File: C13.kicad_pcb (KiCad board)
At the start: 2 copper layers, 80 x 40.1 mm, 120 parts, among them IC1 74HC595BQ,115, IC2 MPM3610AGQV-P, IC9 THVD1450DRBR, J1 V24, J2 Conn_02x04, J3 Conn_02x03, J4 Screw_Terminal_01x04, J5 UDPI, J6 Screw_Terminal_01x04, J7 Screw_Terminal_01x02, K1 G6K-2, Q1 BC848W, Q5 BC857BS, U1 AVR-64DA48, U10 INA181-A1, U11 INA381, U12 INA381, U13 INA181-A1, U14 INA381, U15 INA381, U16 INA181-A4, U2 MIC5235-3.3, U3 INA181-A1, U4 KA78M05_TO252, U5 INA381, U6 INA381, U7 INA181-A1, U8 INA381-A2, U9 INA381, X1 ASE-xxxMHz

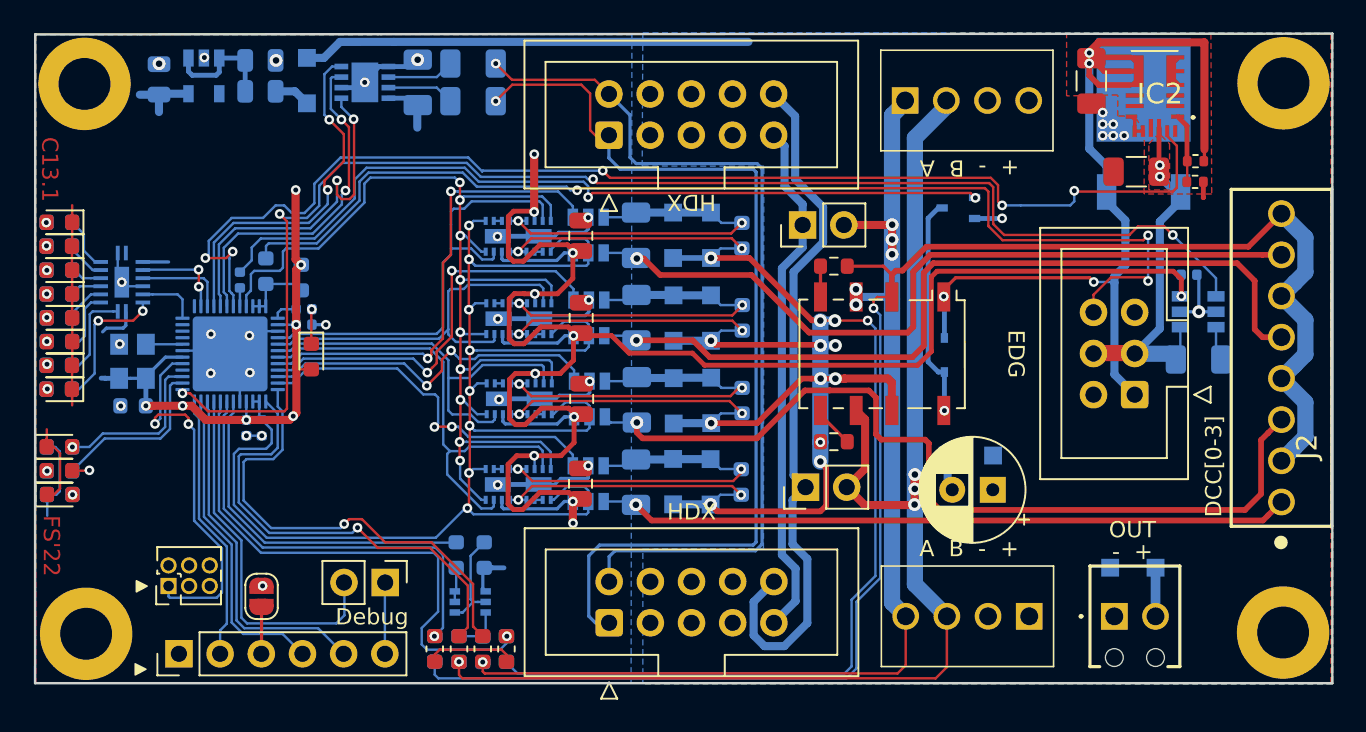
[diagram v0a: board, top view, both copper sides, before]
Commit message: mod: conversion to KiCad 9
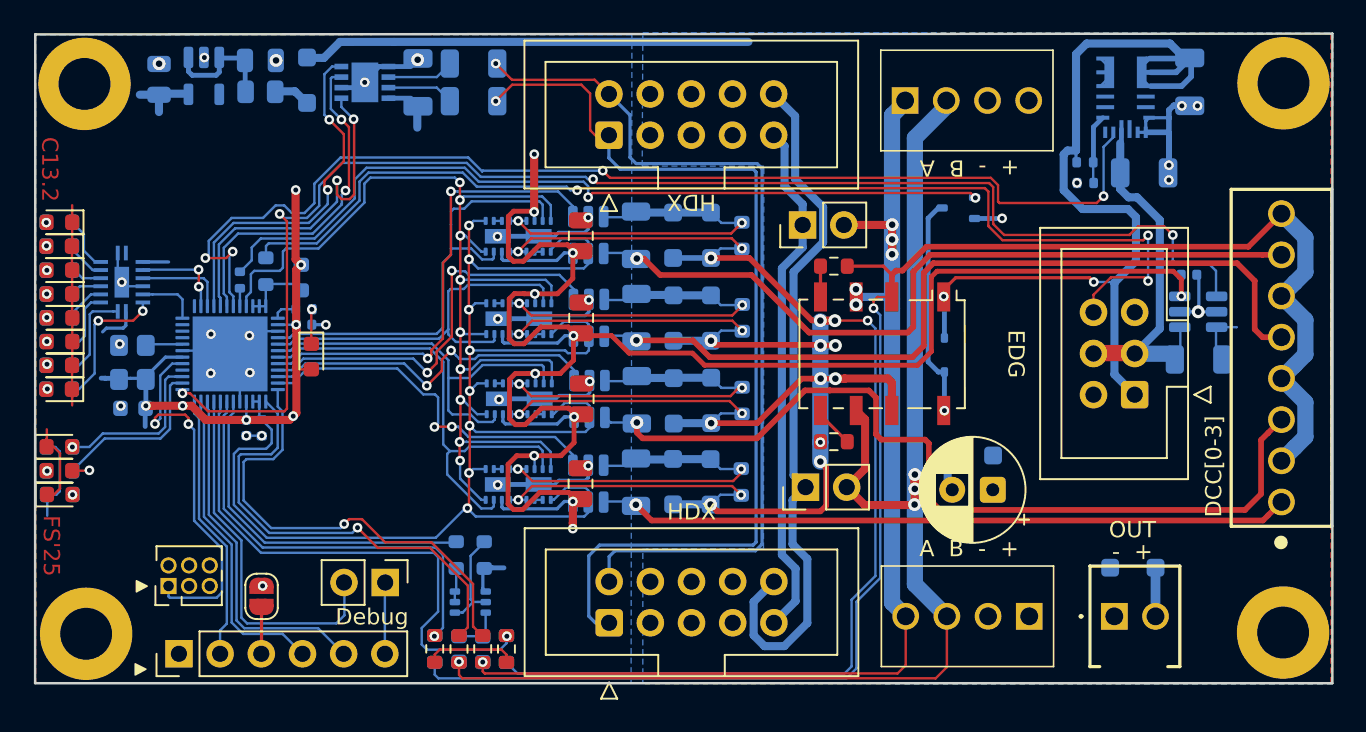
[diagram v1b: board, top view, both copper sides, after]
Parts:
- removed Q5: BC857BS, Package_TO_SOT_SMD:SOT-363_SC-70-6
- removed U4: KA78M05_TO252, Package_TO_SOT_SMD:TO-252-2
- added Q3: BC857BS, Package_TO_SOT_SMD:SOT-363_SC-70-6, B.Cu at (77.0, -13.5)
- C.0.0, C.0.1: value Conn_01x10 -> FDX daisy chain
- C10: value 1u/6V -> 100n
- C11, C13, C6: value 1u -> 100n
- C7: value 22u/25V -> 22u/10V; moved to B.Cu
- C8, IC2: moved to B.Cu
- D1: value D -> SS34FA
- D23, D24: value D_Schottky_Small -> SS34FA
- D25: value D_Schottky -> Schottky
- D30, D31: value D -> Schottky
- J2: value Conn_02x04 -> DCC connector
- J3: value Conn_02x03 -> EDG connector
- J4, J6: value Screw_Terminal_01x04 -> Power Daisy Chain; footprint _Samac:1725672 -> RTB:1725672
- J7: value Screw_Terminal_01x02 -> Power Output; footprint _Samac:1725656 -> RTB:1725656
- R10, R11, R12, R13, R14, R15, R16, R9: value 10k -> 4.7k
- R17, R19, R2, R22: value .1 -> 0.1
- R29: value 160k -> 68k; moved to B.Cu
- R30: value 30.1k -> 13k; moved to B.Cu
- R4, R72: value 47k -> 3.3k
- R5: value 2.2k -> 3.3k
- R6: value 6.8k -> 3.3k
- U8: value INA381-A2 -> INA381
- moved R29 6.82 mm to (114.9, -40.6), turned to 180 degrees
- moved R30 6.77 mm to (115.0, -39.3), turned to 0 degrees
- moved C7 6.07 mm to (121.4, -45.5)
- moved IC2 1.82 mm to (117.4, -44.9), turned to 0 degrees
- moved C8 0.49 mm to (118.6, -39.9), turned to 0 degrees
- moved C11 0.16 mm to (56.2, -25.4)
- moved X1 0.07 mm to (56.2, -28.2)
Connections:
- IC1 pad 9: (no net) -> unconnected-(IC1-Q7S-Pad9)
- IC2 pad 10: (no net) -> unconnected-(IC2-NC_1-Pad10)
- IC2 pad 11: (no net) -> unconnected-(IC2-BST-Pad11)
- IC2 pad 15: (no net) -> unconnected-(IC2-NC_2-Pad15)
- IC2 pad 18: (no net) -> unconnected-(IC2-PG-Pad18)
- IC2 pad 2: (no net) -> unconnected-(IC2-VCC-Pad2)
- IC2 pad 3: (no net) -> unconnected-(IC2-AGND-Pad3)
- J5 pad 3: (no net) -> unconnected-(J5-Pin_3-Pad3)
- J5 pad 4: (no net) -> unconnected-(J5-Pin_4-Pad4)
- J5 pad 5: (no net) -> unconnected-(J5-Pin_5-Pad5)
- U1 pad 1: (no net) -> unconnected-(U1-PA5-Pad1)
- U1 pad 40: (no net) -> unconnected-(U1-PF6/~{RESET}-Pad40)
- U1 pad 45: (no net) -> unconnected-(U1-PA1-Pad45)
- U1 pad 46: (no net) -> unconnected-(U1-PA2-Pad46)
- U1 pad 47: (no net) -> unconnected-(U1-PA3-Pad47)
- U2 pad 4: (no net) -> unconnected-(U2-BP-Pad4)
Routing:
- net GND: track 81.3 -> 89.3 mm, vias 31 -> 30
- net EDG.pwr.ena: track 75.9 -> 71.1 mm, vias 5 -> 4
- net +5V: track 63.8 -> 60.6 mm, vias 4 -> 2
- net +3V3: track 179.8 -> 181.4 mm
- net Vbst: track 29.5 -> 31.1 mm
- net EDG.pwr: track 22.9 -> 24.2 mm, vias 2 -> 0
- net EDG.isens: track 85.2 -> 86.4 mm
- net DCC-b-F: track 177.4 -> 178.3 mm
- net REF: track 93.9 -> 94.4 mm
- removed copper zone on F.Cu, net EDG.pwr
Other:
- net class Default removed
- net class Power removed
- rule pad_to_mask_clearance: 0.2 -> 0
- board text added: "C13.2"
- board text added: "FS'25"
- board text removed: "C13.1"
- board text removed: "FS'22"

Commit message: mod: conversion to KiCad 9
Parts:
- IC2: value MPM3610AGQV-P -> MPM3610AGQV
- Q1: value BC848W -> BC848
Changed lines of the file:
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@@
 	(title_block
 		(title "RTB C13 Module")
-		(date "2025-10-13")
+		(date "2025-10-14")
 		(rev "2")
 		(company "Frank Schumacher")
@@
 			)
 		)
-		(property "Value" "BC848W"
+		(property "Value" "BC848"
 			(at -0.05 -2.05 0)
 			(layer "B.Fab")
@@
 			)
 		)
-		(property "Description" "100MHz 100mA 110@2mA,5V 15nA 200mV 200mW 30V 5V NPN SOT-323 Bipolar (BJT) ROHS"
+		(property "Description" "-65℃~+150℃ 100mA 100nA 200@2mA,5V 200MHz 200mW 250mV 30V NPN SOT-323 Bipolar (BJT) ROHS"
 			(at 0 0 180)
 			(layer "F.Fab")
@@
 			)
 		)
-		(property "LCSC Part #" "C549496"
+		(property "LCSC Part #" "C600677"
 			(at 0 0 180)
 			(unlocked yes)
@@
 			)
 		)
-		(property "Value" "MPM3610AGQV-P"
+		(property "Value" "MPM3610AGQV"
 			(at -0.3 0.15 0)
 			(layer "B.SilkS")
@@
 			)
 		)
-		(property "LCSC Part #" "C6097430"
+		(property "LCSC Part #" "C5173872"
 			(at 0 0 180)
 			(unlocked yes)

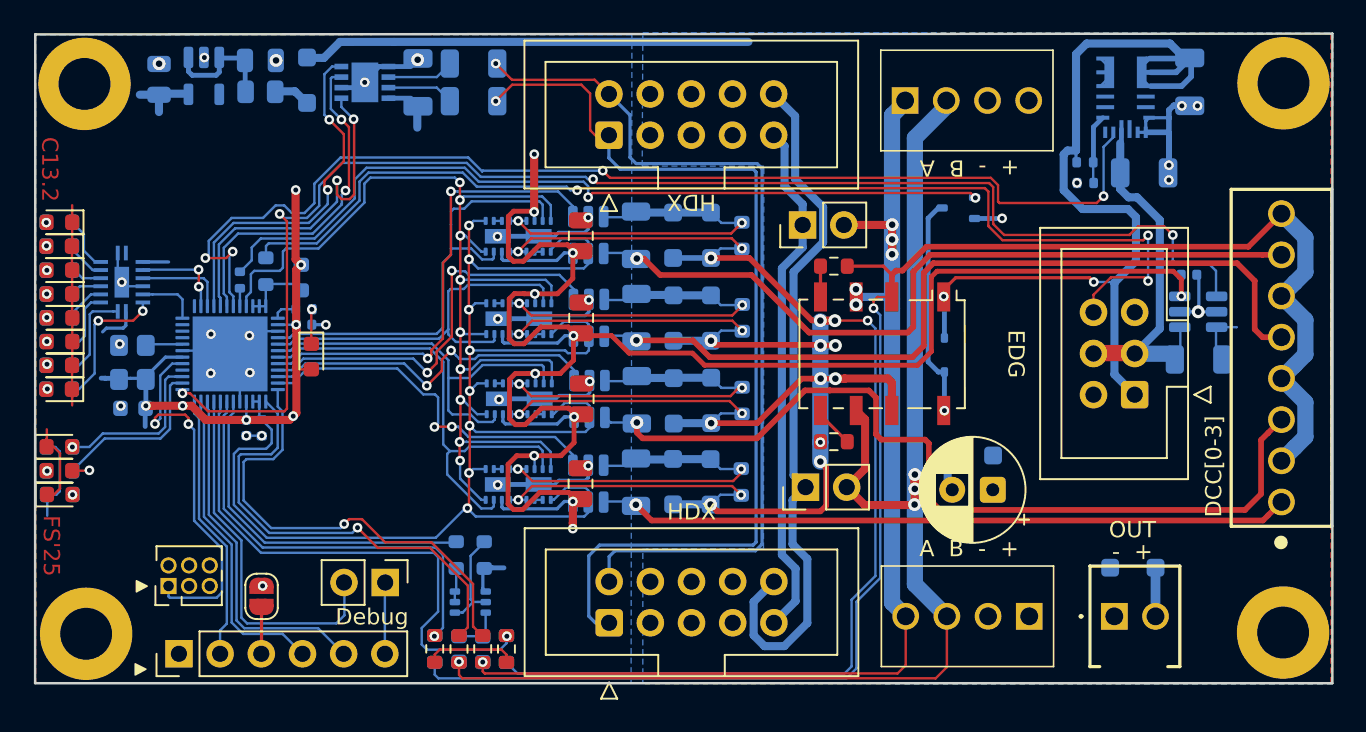
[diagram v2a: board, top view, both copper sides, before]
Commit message: mod: conversion to KiCad 9
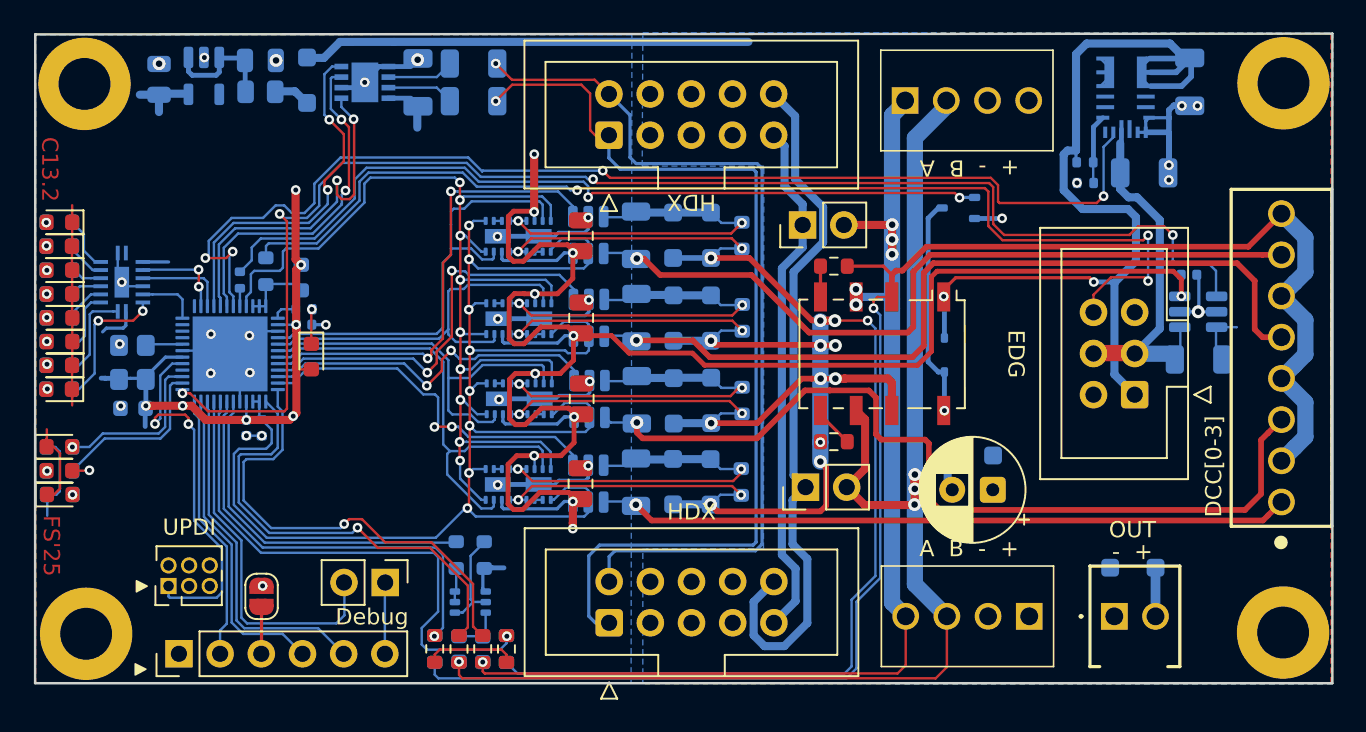
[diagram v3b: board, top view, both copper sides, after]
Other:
- board text added: "UPDI"
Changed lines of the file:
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@@
 			(at 0 0 0)
 			(layer "B.SilkS")
+			(hide yes)
 			(effects
 				(font
@@
 			(at 0 0 270)
 			(layer "B.SilkS")
-			(hide yes)
 			(effects
 				(font
@@
 			)
 		)
-		(property "Description" "-55℃~+155℃ 100mW 1kΩ 75V Thick Film Resistor ±1% ±100ppm/℃ 0603 Chip Resistor - Surface Mount ROHS"
+		(property "Description" "-55℃~+155℃ 1kΩ 50V 62.5mW Thick Film Resistor ±1% ±100ppm/℃ 0402 Chip Resistor - Surface Mount ROHS"
 			(at 0 0 90)
 			(layer "F.Fab")
@@
 			)
 		)
-		(property "LCSC Part #" "C21190"
+		(property "LCSC Part #" "C11702"
 			(at 0 0 270)
 			(unlocked yes)
@@
 			)
 		)
-		(property "Description" "-55℃~+155℃ 100mW 1kΩ 75V Thick Film Resistor ±1% ±100ppm/℃ 0603 Chip Resistor - Surface Mount ROHS"
+		(property "Description" "-55℃~+155℃ 1kΩ 50V 62.5mW Thick Film Resistor ±1% ±100ppm/℃ 0402 Chip Resistor - Surface Mount ROHS"
 			(at 0 0 90)
 			(layer "F.Fab")
@@
 			)
 		)
-		(property "LCSC Part #" "C21190"
+		(property "LCSC Part #" "C11702"
 			(at 0 0 270)
 			(unlocked yes)
@@
 		)
 	)
+	(gr_text "UPDI"
+		(at 59.7 -18.075 0)
+		(layer "F.SilkS")
+		(effects
+			(font
+				(size 1 1)
+				(thickness 0.15)
+			)
+		)
+	)
 	(gr_text "DCC[0-3]"
 		(at 122.875 -21.825 90)
@@
 		(start 115.475 -33.2)
 		(end 116.7 -33.2)
-		(width 0.15)
+		(width 0.3)
 		(layer "B.Cu")
 		(net 49)
@@
 	)
 	(segment
-		(start 107.873521 -38.687019)
+		(start 106.912981 -38.687019)
 		(end 84.559419 -38.687019)
 		(width 0.15)
@@
 	)
 	(segment
-		(start 108.17352 -38.38702)
-		(end 107.873521 -38.687019)
+		(start 107.2 -38.4)
+		(end 106.912981 -38.687019)
 		(width 0.15)
 		(layer "F.Cu")
@@
 	)
 	(via
-		(at 108.17352 -38.38702)
+		(at 107.2 -38.4)
 		(size 0.6)
 		(drill 0.3)
@@
 	)
 	(segment
+		(start 108.12704 -38.41472)
+		(end 107.21472 -38.41472)
+		(width 0.2)
+		(layer "B.Cu")
+		(net 93)
+	)
+	(segment
 		(start 62.82182 -33.80726)
 		(end 63.55 -34.53544)
@@
 		(width 0.15)
 		(layer "B.Cu")
+		(net 93)
+	)
+	(segment
+		(start 107.21472 -38.41472)
+		(end 107.2 -38.4)
+		(width 0.15)
+		(layer "B.Cu")
